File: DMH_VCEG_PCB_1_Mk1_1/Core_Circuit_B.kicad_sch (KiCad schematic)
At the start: 111 parts, among them J24 Conn_01x06_PinHeader, J25 Conn_01x10_PinHeader, J26 Conn_01x10_PinHeader, J27 Conn_01x10_PinHeader, Q17 BC558, Q18 BC558, Q19 BC548, Q20 BC548, Q21 BS170, Q22 BS170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

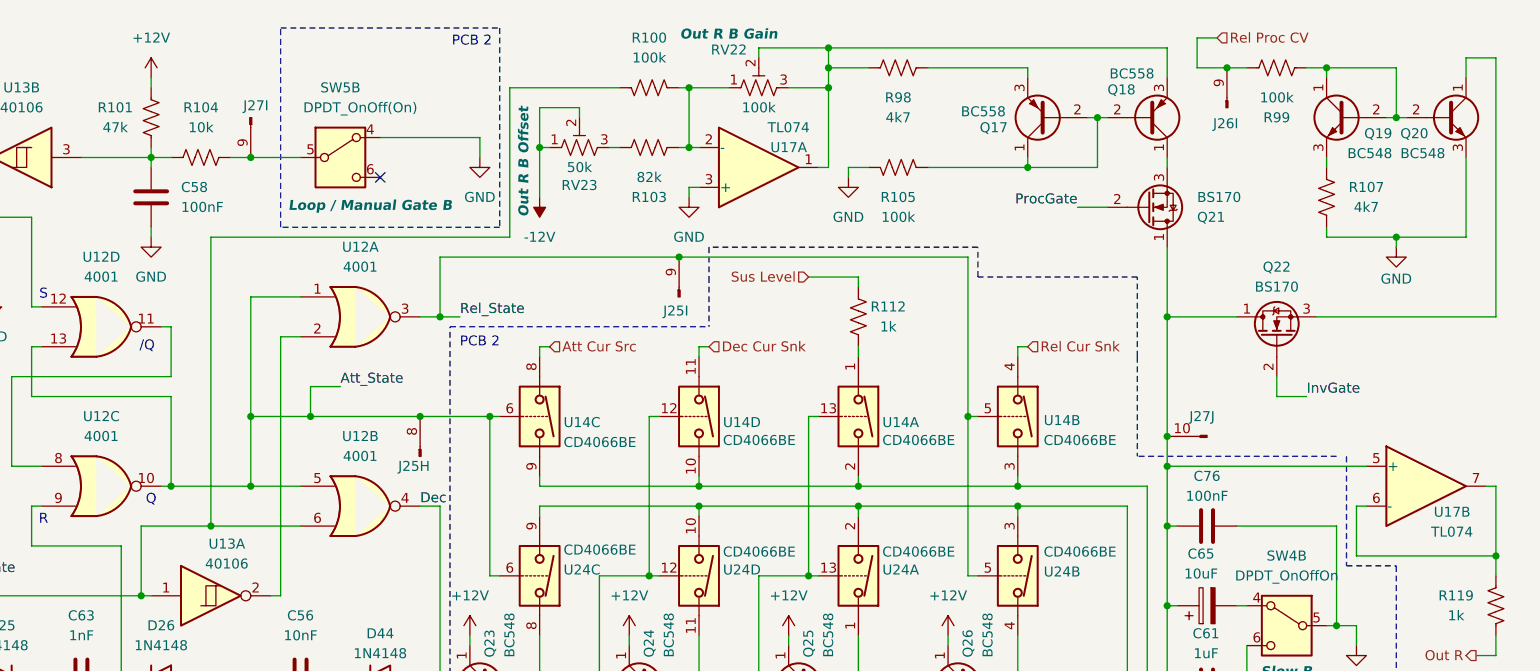
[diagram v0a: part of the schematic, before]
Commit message: Copied Out R redesign to Circuit B
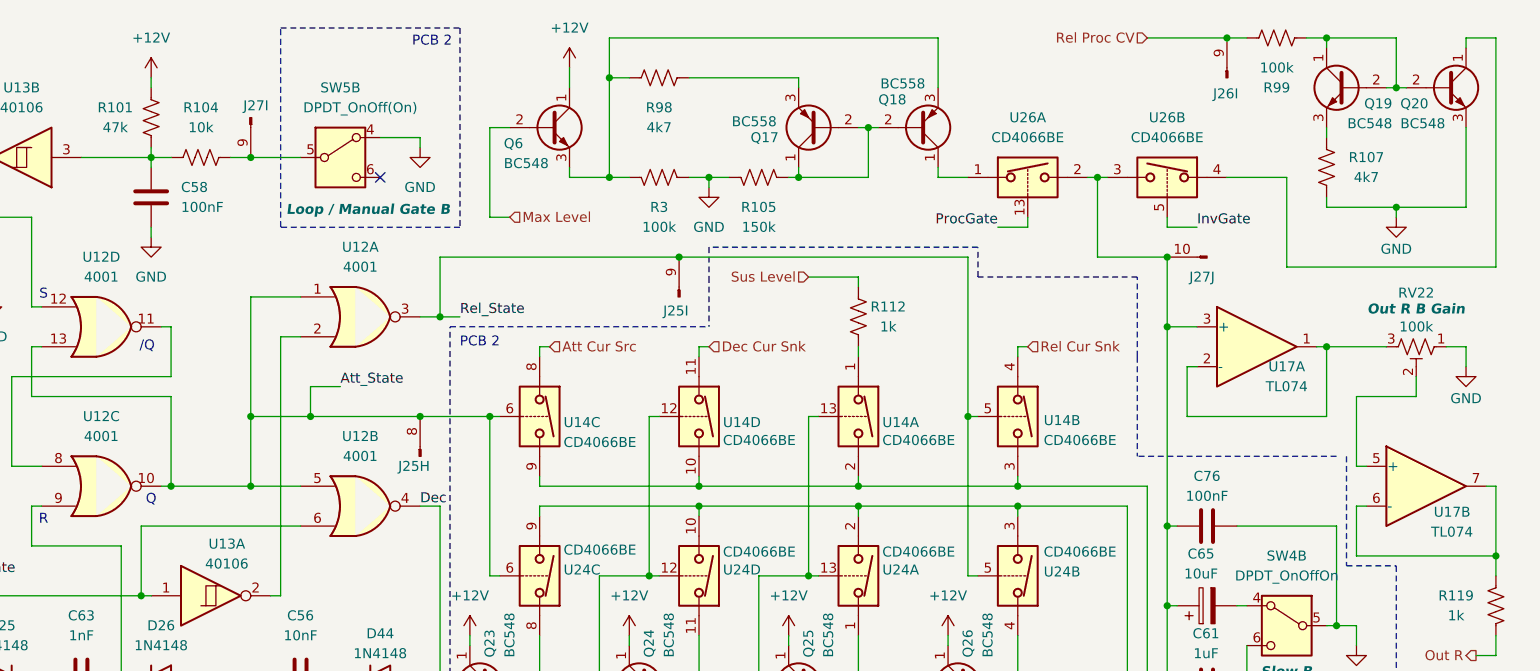
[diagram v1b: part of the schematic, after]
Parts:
- removed Q21, Q22: BS170, Package_TO_SOT_THT:TO-92_Inline, symbol Transistor_FET:BS170
- removed R100: 100k, Resistor_THT:R_Axial_DIN0207_L6.3mm_D2.5mm_P7.62mm_Horizontal, symbol Device:R_US
- removed R103: 82k, Resistor_THT:R_Axial_DIN0207_L6.3mm_D2.5mm_P7.62mm_Horizontal, symbol Device:R_US
- removed RV23: 50k, Potentiometer_THT:Potentiometer_Bourns_3296W_Vertical, symbol Device:R_Potentiometer_Trim_US
- added Q6: BC548, Package_TO_SOT_THT:TO-92L_Inline_Wide, symbol Transistor_BJT:BC548
- added R3: 100k, Resistor_THT:R_Axial_DIN0207_L6.3mm_D2.5mm_P7.62mm_Horizontal, symbol Device:R_US
- added U26: CD4066BE, Package_DIP:DIP-14_W7.62mm_Socket, symbol Analog_Switch:CD4066BE
- R105: value 100k -> 150k
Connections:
- net +12V: now also Q6.1 (C)
- net GND: now also RV22.1, R3.1; no longer U17.3 (+)
- net InvGate: now also U26.5
- net Max Level: now also Q6.2 (B)
- net ProcGate: now also U26.13
- net at C61.2, C65.1, C76.2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: now also U17.3 (+), U26.2, U26.3; no longer U17.5 (+)
- net at Q18.1 (C): now also U26.1
- net at Q20.1 (C): now also U26.4
- net at U17.2 (-): now also RV22.3, U17.1; no longer RV22.1
- new net: Q18.3 (E), Q6.3 (E), R3.2, R98.1
- new net: RV22.2, U17.5 (+)
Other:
- moved on the sheet: J26I, J27J, Q17, Q18, Q19, Q20, R105, R107, R98, R99, RV22, U17A
